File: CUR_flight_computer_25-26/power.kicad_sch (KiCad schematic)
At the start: 0 parts

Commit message: Setup Power
Setup:
- current sense
- voltage sense
- LDO
- power switching
- bat terminals
- screw terminals

Still needs:
- LEDs
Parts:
- added C13, C?: 1u, symbol Device:C_Small
- added J1, J?: XT30PW-M, Connector_AMASS_XT:AMASS_XT30PW-M_1x02_P2.50mm_Horizontal, symbol Connector:Conn_01x02_Pin
- added J2, J?: Screw_Terminal_01x02, symbol Connector:Screw_Terminal_01x02
- added R1, R?: 10k, symbol Device:R_Small_US
- added R2, R4: 18k, symbol Device:R_Small_US
- added R3, R5: 47k, symbol Device:R_Small_US
- added R6: 1mOhm 1W, symbol Device:R_Small_US
- added R?: 5mOhm 1W, symbol Device:R_Small_US
- added U1, U?: ZXCT180A4W5, Package_TO_SOT_SMD:SOT-23-5, symbol DI_ZXCT180:ZXCT180A4
- added U?: BU33SD5, BUxxSD5:SSOP5_ROM, symbol BUxxSD5:BU33SD5
- added U?: LM66200, Package_TO_SOT_SMD:SOT-583-8, symbol LM66200:LM66200
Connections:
- new net: R?.2, U?.4 (~{ON})
- new net +3V3: C13.1, R1.2, U1.5 (VS), U?.5 (VOUT), U?.5 (VS)
- new net +BATT: R?.2, U?.4 (IN-), U?.6 (VIN2)
- new net BATT_MEAS: J?.1 (Pin_1), R2.2, R?.1, U?.3 (IN+)
- new net BATT_PYRO: R6.2, U1.4 (IN-)
- new net BATT_SENSE: R2.1, R3.2
- new net BATT_SWITCH: J?.2 (Pin_2), J?.2 (Pin_2)
- new net GND: C13.2, C?.2, J1.1 (Pin_1), J?.1 (Pin_1), R3.1, R5.1, R?.1, U1.2 (GND), U?.1 (GND), U?.2 (GND), U?.2 (GND), U?.5 (GND)
- new net I_SENSE: U?.1 (OUT)
- new net I_SENSE_PYRO: U1.1 (OUT)
- new net LDO_IN: C?.1, U?.1 (VIN), U?.2 (VOUT), U?.3 (STDBY), U?.7 (VOUT)
- new net LM660_ST: R1.1, U?.8 (ST)
- new net PYRO_BATT_MEAS: J2.1 (Pin_1), R4.2, R6.1, U1.3 (IN+)
- new net PYRO_BATT_SENSE: R4.1, R5.2
- new net PYRO_BATT_SWITCH: J1.2 (Pin_2), J2.2 (Pin_2)
- new net VBUS: U?.3 (VIN1)
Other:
- note added: "12-bit ADC"
- note added: "Current pulled - 500ma"
- note added: "VBUS - USB Voltage in BATT+ - main battery BATT_PYRO - pyro battery"
- note added: "higher, more voltage drop, more current sense states"

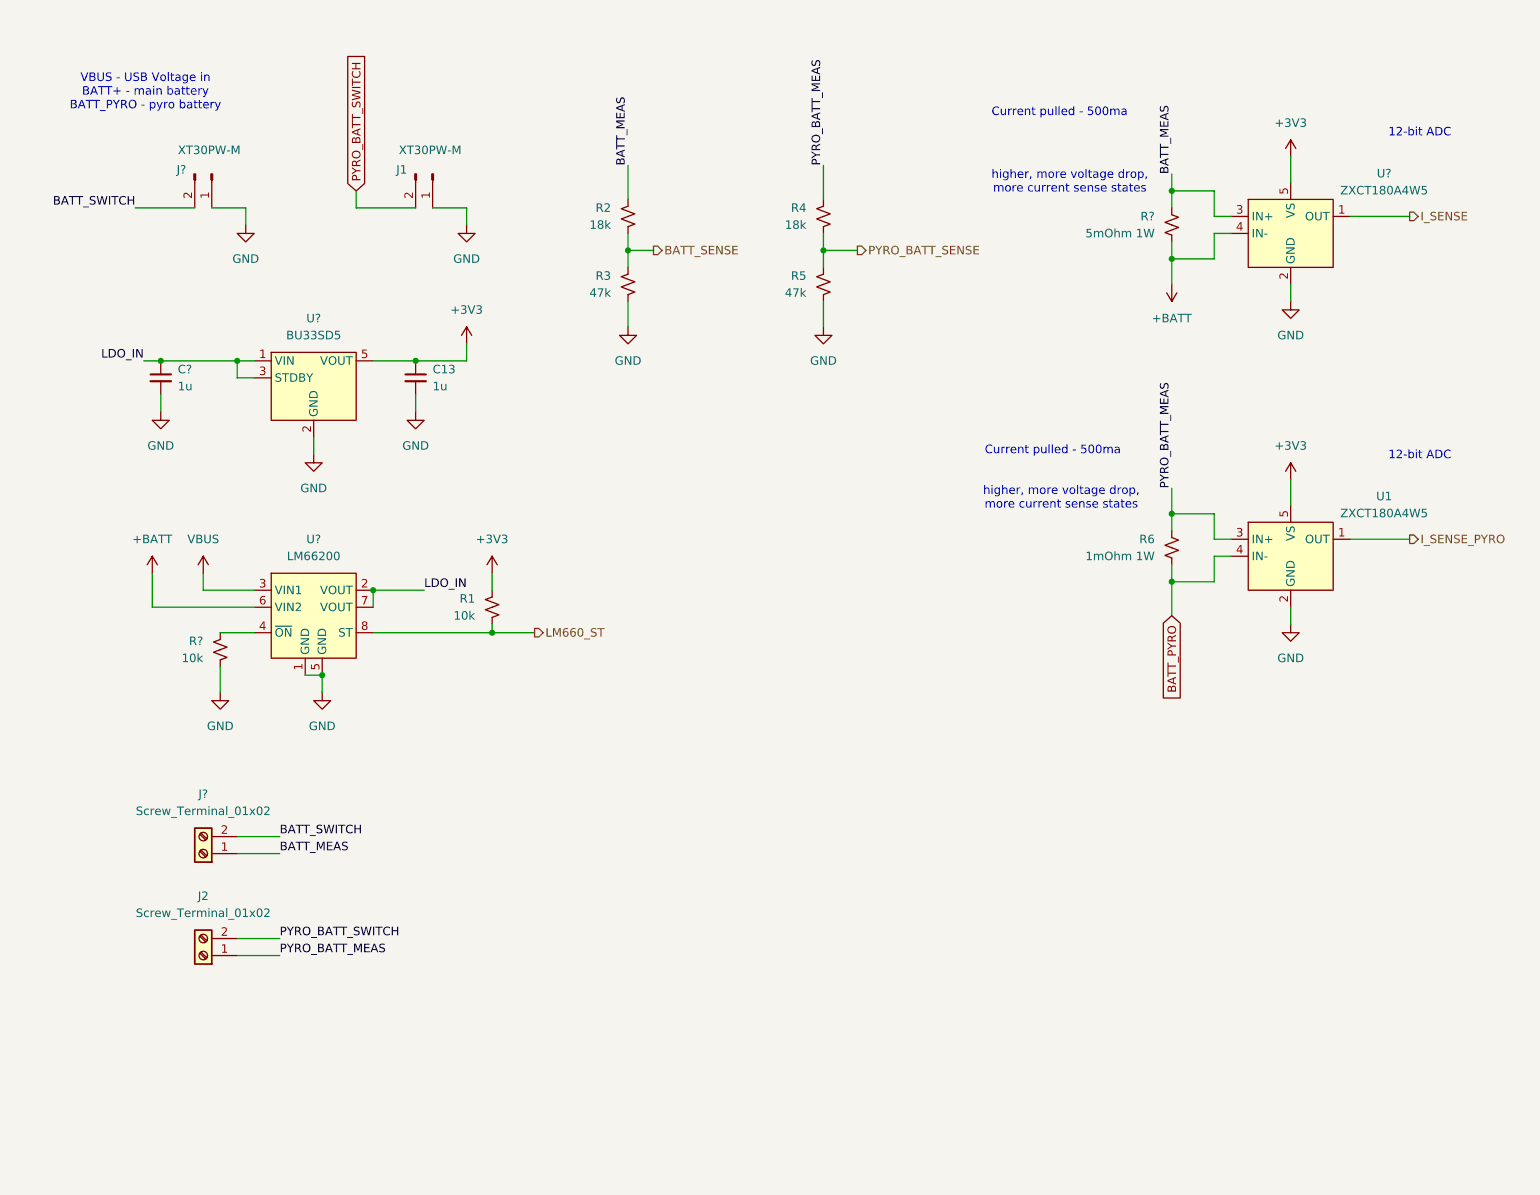
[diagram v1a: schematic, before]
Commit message: added buttons, leds on power
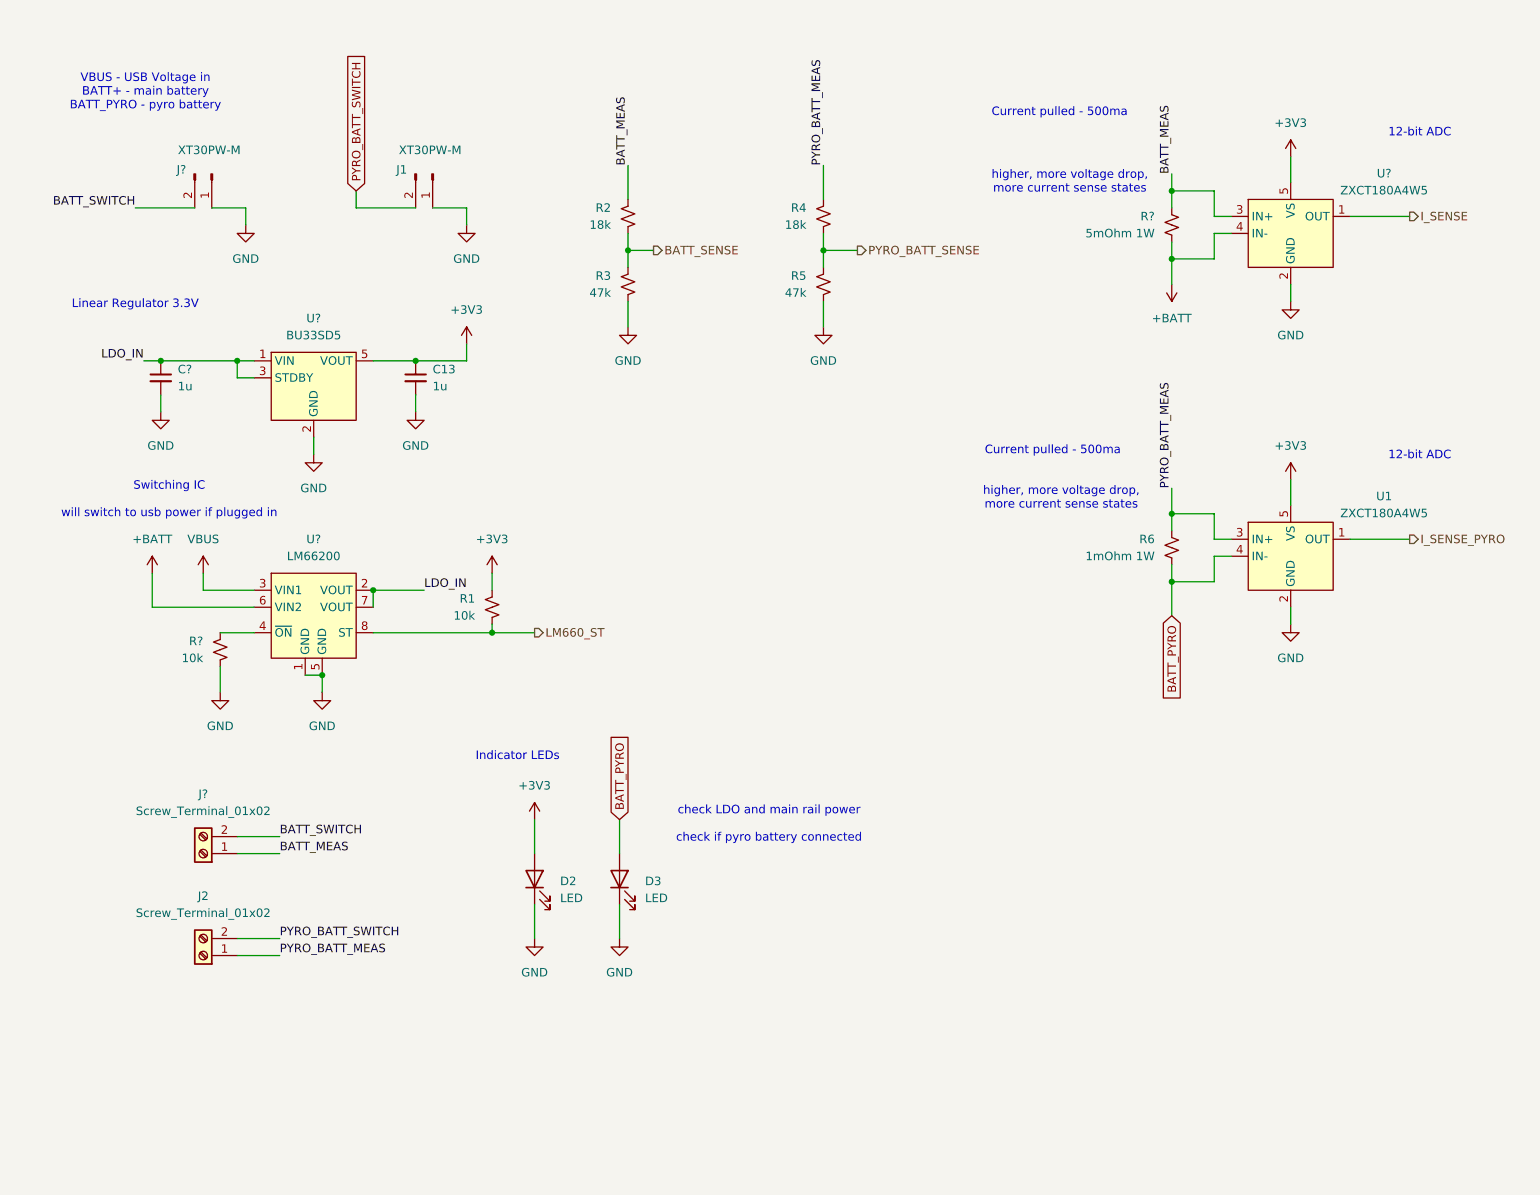
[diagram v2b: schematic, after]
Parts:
- added D2, D3: LED, symbol Device:LED
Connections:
- net +3V3: now also D2.2 (A)
- net BATT_PYRO: now also D3.2 (A)
- net GND: now also D2.1 (K), D3.1 (K)
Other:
- note added: "Indicator LEDs"
- note added: "Linear Regulator 3.3V"
- note added: "Switching IC will switch to usb power if plugged in"
- note added: "check LDO and main rail power check if pyro battery connected"

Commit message: led fixes and such
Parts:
- added R43, R7: 150, symbol Device:R_Small_US
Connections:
- net +3V3: now also R7.2; no longer D2.2 (A)
- net BATT_PYRO: now also R43.2; no longer D3.2 (A)
- new net: D2.2 (A), R7.1
- new net: D3.2 (A), R43.1
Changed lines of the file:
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@@
 	(text "Indicator LEDs"
 		(exclude_from_sim no)
-		(at 87.63 121.412 0)
+		(at 78.486 116.586 0)
 		(effects
 			(font
@@
 	(wire
 		(pts
+			(xy 90.17 128.27) (xy 90.17 124.46)
+		)
+		(stroke
+			(width 0)
+			(type default)
+		)
+	)
+	(wire
+		(pts
 			(xy 212.09 40.64) (xy 220.98 40.64)
 		)
@@
 	(wire
 		(pts
-			(xy 90.17 135.89) (xy 90.17 130.81)
+			(xy 90.17 135.89) (xy 90.17 133.35)
+		)
+		(stroke
+			(width 0)
+			(type default)
+		)
+	)
+	(wire
+		(pts
+			(xy 102.87 128.27) (xy 102.87 123.19)
 		)
 		(stroke
@@
 	(wire
 		(pts
-			(xy 102.87 135.89) (xy 102.87 130.81)
+			(xy 102.87 135.89) (xy 102.87 133.35)
 		)
 		(stroke
@@
 	(global_label "BATT_PYRO"
 		(shape input)
-		(at 102.87 130.81 90)
+		(at 102.87 123.19 90)
 		(fields_autoplaced yes)
 		(effects
@@
 		)
 		(property "Intersheetrefs" "${INTERSHEET_REFS}"
-			(at 102.87 117.6043 90)
+			(at 102.87 109.9843 90)
 			(effects
 				(font
@@
 	(symbol
 		(lib_id "power:+3V3")
-		(at 90.17 130.81 0)
+		(at 90.17 124.46 0)
 		(unit 1)
 		(exclude_from_sim no)
@@
 		(fields_autoplaced yes)
 		(property "Reference" "#PWR057"
-			(at 90.17 134.62 0)
+			(at 90.17 128.27 0)
 			(effects
 				(font
@@
 		)
 		(property "Value" "+3V3"
-			(at 90.17 125.73 0)
+			(at 90.17 119.38 0)
 			(effects
 				(font
@@
 		)
 		(property "Footprint" ""
-			(at 90.17 130.81 0)
+			(at 90.17 124.46 0)
 			(effects
 				(font
@@
 		)
 		(property "Datasheet" ""
-			(at 90.17 130.81 0)
+			(at 90.17 124.46 0)
 			(effects
 				(font
@@
 		)
 		(property "Description" "Power symbol creates a global label with name \"+3V3\""
-			(at 90.17 130.81 0)
+			(at 90.17 124.46 0)
 			(effects
 				(font
@@
 	)
 	(symbol
+		(lib_id "Device:R_Small_US")
+		(at 102.87 130.81 0)
+		(mirror x)
+		(unit 1)
+		(exclude_from_sim no)
+		(in_bom yes)
+		(on_board yes)
+		(dnp no)
+		(fields_autoplaced yes)
+		(property "Reference" "R43"
+			(at 100.33 129.5399 0)
+			(effects
+				(font
+					(size 1.27 1.27)
+				)
+				(justify right)
+			)
+		)
+		(property "Value" "150"
+			(at 100.33 132.0799 0)
+			(effects
+				(font
+					(size 1.27 1.27)
+				)
+				(justify right)
+			)
+		)
+		(property "Footprint" ""
+			(at 102.87 130.81 0)
+			(effects
+				(font
+					(size 1.27 1.27)
+				)
+				(hide yes)
+			)
+		)
+		(property "Datasheet" "~"
+			(at 102.87 130.81 0)
+			(effects
+				(font
+					(size 1.27 1.27)
+				)
+				(hide yes)
+			)
+		)
+		(property "Description" "Resistor, small US symbol"
+			(at 102.87 130.81 0)
+			(effects
+				(font
+					(size 1.27 1.27)
+				)
+				(hide yes)
+			)
+		)
+		(pin "1"
+		)
+		(pin "2"
+		)
+		(instances
+			(project "CUR_flight_computer_25-26"
+				(path "/bf7761cc-1b32-4d86-809c-5f027005229b/1df302fb-2dab-4194-ae63-c7585125533e"
+					(reference "R43")
+					(unit 1)
+				)
+			)
+		)
+	)
+	(symbol
 		(lib_id "power:+3V3")
 		(at 80.01 59.69 0)
@@
 					(unit 1)
 				)
+			)
+		)
+	)
+	(symbol
+		(lib_id "Device:R_Small_US")
+		(at 90.17 130.81 0)
+		(mirror x)
+		(unit 1)
+		(exclude_from_sim no)
+		(in_bom yes)
+		(on_board yes)
+		(dnp no)
+		(fields_autoplaced yes)
+		(property "Reference" "R7"
+			(at 87.63 129.5399 0)
+			(effects
+				(font
+					(size 1.27 1.27)
+				)
+				(justify right)
+			)
+		)
+		(property "Value" "150"
+			(at 87.63 132.0799 0)
+			(effects
+				(font
+					(size 1.27 1.27)
+				)
+				(justify right)
+			)
+		)
+		(property "Footprint" ""
+			(at 90.17 130.81 0)
+			(effects
+				(font
+					(size 1.27 1.27)
+				)
+				(hide yes)
+			)
+		)
+		(property "Datasheet" "~"
+			(at 90.17 130.81 0)
+			(effects
+				(font
+					(size 1.27 1.27)
+				)
+				(hide yes)
+			)
+		)
+		(property "Description" "Resistor, small US symbol"
+			(at 90.17 130.81 0)
+			(effects
+				(font
+					(size 1.27 1.27)
+				)
+				(hide yes)
+			)
+		)
+		(pin "1"
+		)
+		(pin "2"
+		)
+		(instances
+			(project "CUR_flight_computer_25-26"
+				(path "/bf7761cc-1b32-4d86-809c-5f027005229b/1df302fb-2dab-4194-ae63-c7585125533e"
+					(reference "R7")
+					(unit 1)
+				)

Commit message: updated all needed fixes
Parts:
- removed J2: Screw_Terminal_01x02, symbol Connector:Screw_Terminal_01x02
- added D3, D4, D5, D6, D7, D8: ESDZV5HS-1BF4, symbol Device:D_TVS_Small
- added J3: Screw_Terminal_01x02, symbol Connector:Screw_Terminal_01x02
- gave numbers to parts that had none: 8
- renumbered C13 to C29, D3 to D10, D2 to D9, J1 to J5, R1 to R11, R7 to R12, R43 to R13, R2 to R14, R3 to R15, R4 to R16, R5 to R17, R6 to R19, U1 to U9
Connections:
- net BATT_MEAS: now also D4.2 (A2)
- net BATT_SWITCH: now also D6.2 (A2)
- net GND: now also D3.1 (A1), D3.2 (A2), D4.1 (A1), D5.1 (A1), D6.1 (A1), D7.1 (A1), D8.1 (A1), D8.2 (A2)
- net PYRO_BATT_MEAS: now also D5.2 (A2), J3.1 (Pin_1)
- net PYRO_BATT_SWITCH: now also D7.2 (A2), J3.2 (Pin_2)
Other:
- moved on the sheet: J4, J5

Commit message: assigned footrpint
need to double check:
- HSE
- Capacitors

for some unknown reason cur kicad library refuses to work
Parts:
- C28, C29: footprint (none) -> Capacitor_SMD:C_0603_1608Metric
- D10, D9: footprint (none) -> LED_SMD:LED_0603_1608Metric
- D3, D4, D5, D6, D7, D8: footprint (none) -> Diode_SMD:D_0201_0603Metric
- J2, J3: footprint (none) -> TerminalBlock_Phoenix:TerminalBlock_Phoenix_PT-1,5-2-5.0-H_1x02_P5.00mm_Horizontal
- R10, R11, R12, R13, R14, R15, R16, R17: footprint (none) -> Resistor_SMD:R_0603_1608Metric
- R18: footprint (none) -> Resistor_SMD:R_1206_3216Metric
- R19: footprint (none) -> Resistor_SMD:R_2010_5025Metric
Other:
- note added: "PA2010FKE7W0R001Z - another expensive resistor"
- note added: "PE1206FKM470R005Z - expensive ass resistor"
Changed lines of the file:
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@@
 		)
 	)
+	(text "PE1206FKM470R005Z\n- expensive ass resistor"
+		(exclude_from_sim no)
+		(at 171.45 49.53 0)
+		(effects
+			(font
+				(size 1.27 1.27)
+			)
+		)
+	)
 	(text "check LDO and main rail power\n\ncheck if pyro battery connected\n"
 		(exclude_from_sim no)
@@
 		)
 	)
+	(text "PA2010FKE7W0R001Z\n- another expensive resistor\n"
+		(exclude_from_sim no)
+		(at 168.148 97.536 0)
+		(effects
+			(font
+				(size 1.27 1.27)
+			)
+		)
+	)
 	(text "Linear Regulator 3.3V"
 		(exclude_from_sim no)
@@
 			)
 		)
-		(property "Footprint" ""
+		(property "Footprint" "Resistor_SMD:R_0603_1608Metric"
 			(at 133.35 40.64 0)
 			(effects
@@
 			)
 		)
-		(property "Footprint" ""
+		(property "Footprint" "TerminalBlock_Phoenix:TerminalBlock_Phoenix_PT-1,5-2-5.0-H_1x02_P5.00mm_Horizontal"
 			(at 40.64 135.89 0)
 			(effects
@@
 			)
 		)
-		(property "Footprint" ""
+		(property "Footprint" "Resistor_SMD:R_2010_5025Metric"
 			(at 185.42 90.17 0)
 			(effects
@@
 			)
 		)
-		(property "Footprint" ""
+		(property "Footprint" "LED_SMD:LED_0603_1608Metric"
 			(at 90.17 139.7 0)
 			(effects
@@
 			)
 		)
-		(property "Footprint" ""
+		(property "Footprint" "Capacitor_SMD:C_0603_1608Metric"
 			(at 72.39 64.77 0)
 			(effects
@@
 			)
 		)
-		(property "Footprint" ""
+		(property "Footprint" "TerminalBlock_Phoenix:TerminalBlock_Phoenix_PT-1,5-2-5.0-H_1x02_P5.00mm_Horizontal"
 			(at 40.64 166.37 0)
 			(effects
@@
 			)
 		)
-		(property "Footprint" ""
+		(property "Footprint" "Diode_SMD:D_0201_0603Metric"
 			(at 54.61 173.99 0)
 			(effects
@@
 			)
 		)
-		(property "Footprint" ""
+		(property "Footprint" "Diode_SMD:D_0201_0603Metric"
 			(at 49.53 173.99 0)
 			(effects
@@
 			)
 		)
-		(property "Footprint" ""
+		(property "Footprint" "LED_SMD:LED_0603_1608Metric"
 			(at 102.87 139.7 0)
 			(effects
@@
 			)
 		)
-		(property "Footprint" ""
+		(property "Footprint" "Diode_SMD:D_0201_0603Metric"
 			(at 54.61 143.51 0)
 			(effects
@@
 			)
 		)
-		(property "Footprint" ""
+		(property "Footprint" "Resistor_SMD:R_0603_1608Metric"
 			(at 104.14 50.8 0)
 			(effects
@@
 			)
 		)
-		(property "Footprint" ""
+		(property "Footprint" "Resistor_SMD:R_0603_1608Metric"
 			(at 104.14 40.64 0)
 			(effects
@@
 			)
 		)
-		(property "Footprint" ""
+		(property "Footprint" "Resistor_SMD:R_0603_1608Metric"
 			(at 83.82 99.06 0)
 			(effects
@@
 			)
 		)
-		(property "Footprint" ""
+		(property "Footprint" "Resistor_SMD:R_0603_1608Metric"
 			(at 43.18 105.41 0)
 			(effects
@@
 			)
 		)
-		(property "Footprint" ""
+		(property "Footprint" "Diode_SMD:D_0201_0603Metric"
 			(at 49.53 143.51 0)
 			(effects
@@
 			)
 		)
-		(property "Footprint" ""
+		(property "Footprint" "Resistor_SMD:R_1206_3216Metric"
 			(at 185.42 41.91 0)
 			(effects
@@
 			)
 		)
-		(property "Footprint" ""
+		(property "Footprint" "Resistor_SMD:R_0603_1608Metric"
 			(at 133.35 50.8 0)
 			(effects
@@
 			)
 		)
-		(property "Footprint" ""
+		(property "Footprint" "Diode_SMD:D_0201_0603Metric"
 			(at 80.01 40.64 0)
 			(effects
@@
 			)
 		)
-		(property "Footprint" ""
+		(property "Footprint" "Diode_SMD:D_0201_0603Metric"
 			(at 46.99 40.64 0)
 			(effects
@@
 			)
 		)
-		(property "Footprint" ""
+		(property "Footprint" "Resistor_SMD:R_0603_1608Metric"
 			(at 102.87 130.81 0)
 			(effects
@@
 			)
 		)
-		(property "Footprint" ""
+		(property "Footprint" "Resistor_SMD:R_0603_1608Metric"
 			(at 90.17 130.81 0)
 			(effects
@@
 			)
 		)
-		(property "Footprint" ""
+		(property "Footprint" "Capacitor_SMD:C_0603_1608Metric"
 			(at 34.29 64.77 0)
 			(effects

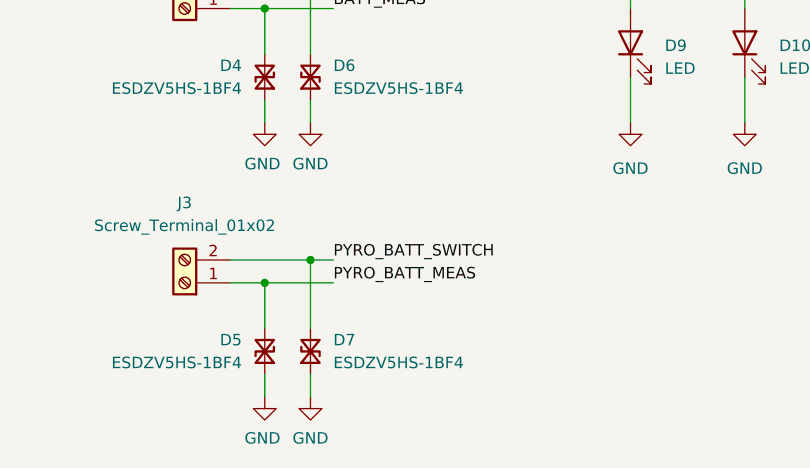
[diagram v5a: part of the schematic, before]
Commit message: most of layout figured out
trouble finding room for power
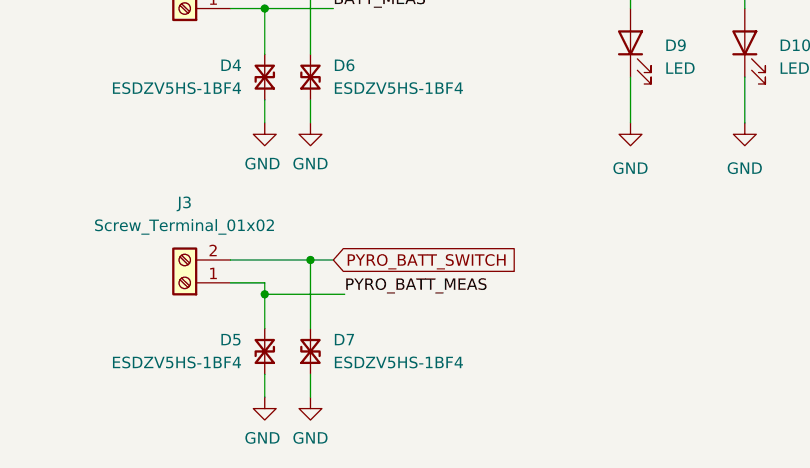
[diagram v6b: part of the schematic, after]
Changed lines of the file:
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@@
+	)
+	(junction
+		(at 49.53 167.64)
+		(diameter 0)
+		(color 0 0 0 0)
 	)
 	(junction
@@
 	)
 	(junction
-		(at 49.53 166.37)
-		(diameter 0)
-		(color 0 0 0 0)
-	)
-	(junction
 		(at 185.42 95.25)
 		(diameter 0)
@@
 	(wire
 		(pts
-			(xy 49.53 166.37) (xy 57.15 166.37)
+			(xy 49.53 167.64) (xy 58.42 167.64)
 		)
 		(stroke
@@
 	(wire
 		(pts
+			(xy 49.53 167.64) (xy 49.53 166.37)
+		)
+		(stroke
+			(width 0)
+			(type default)
+		)
+	)
+	(wire
+		(pts
 			(xy 191.77 95.25) (xy 185.42 95.25)
 		)
@@
 	(wire
 		(pts
-			(xy 49.53 171.45) (xy 49.53 166.37)
+			(xy 49.53 171.45) (xy 49.53 167.64)
 		)
 		(stroke
@@
 		)
 	)
-	(label "PYRO_BATT_SWITCH"
-		(at 57.15 163.83 0)
-		(effects
-			(font
-				(size 1.27 1.27)
-			)
-			(justify left bottom)
-		)
-	)
 	(label "PYRO_BATT_MEAS"
-		(at 57.15 166.37 0)
+		(at 58.42 167.64 0)
 		(effects
 			(font
@@
 			(effects
 				(font
+					(size 1.27 1.27)
+				)
+				(justify left)
+				(hide yes)
+			)
+		)
+	)
+	(global_label "PYRO_BATT_SWITCH"
+		(shape input)
+		(at 57.15 163.83 0)
+		(fields_autoplaced yes)
+		(effects
+			(font
+				(size 1.27 1.27)
+			)
+			(justify left)
+		)
+		(property "Intersheetrefs" "${INTERSHEET_REFS}"
+			(at 78.1571 163.83 0)
+			(effects
+				(font

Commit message: routing updates
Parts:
- J4, J5: footprint Connector_AMASS_XT:AMASS_XT30PW-M_1x02_P2.50mm_Horizontal -> Connector_AMASS:AMASS_XT30U-M_1x02_P5.0mm_Vertical
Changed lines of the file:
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@@
 			)
 		)
-		(property "Footprint" "Connector_AMASS_XT:AMASS_XT30PW-M_1x02_P2.50mm_Horizontal"
+		(property "Footprint" "Connector_AMASS:AMASS_XT30U-M_1x02_P5.0mm_Vertical"
 			(at 74.93 31.75 0)
 			(effects
@@
 			)
 		)
-		(property "Footprint" "Connector_AMASS_XT:AMASS_XT30PW-M_1x02_P2.50mm_Horizontal"
+		(property "Footprint" "Connector_AMASS:AMASS_XT30U-M_1x02_P5.0mm_Vertical"
 			(at 41.91 31.75 0)
 			(effects
